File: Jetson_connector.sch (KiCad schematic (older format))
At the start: 24 parts, among them IC2 AT24MAC402-MAHM-T, IC6 SN74AVC1T45DCKT, J2 QTH-060-01-L-D-A, U2 SN74AVC2T45DCUR

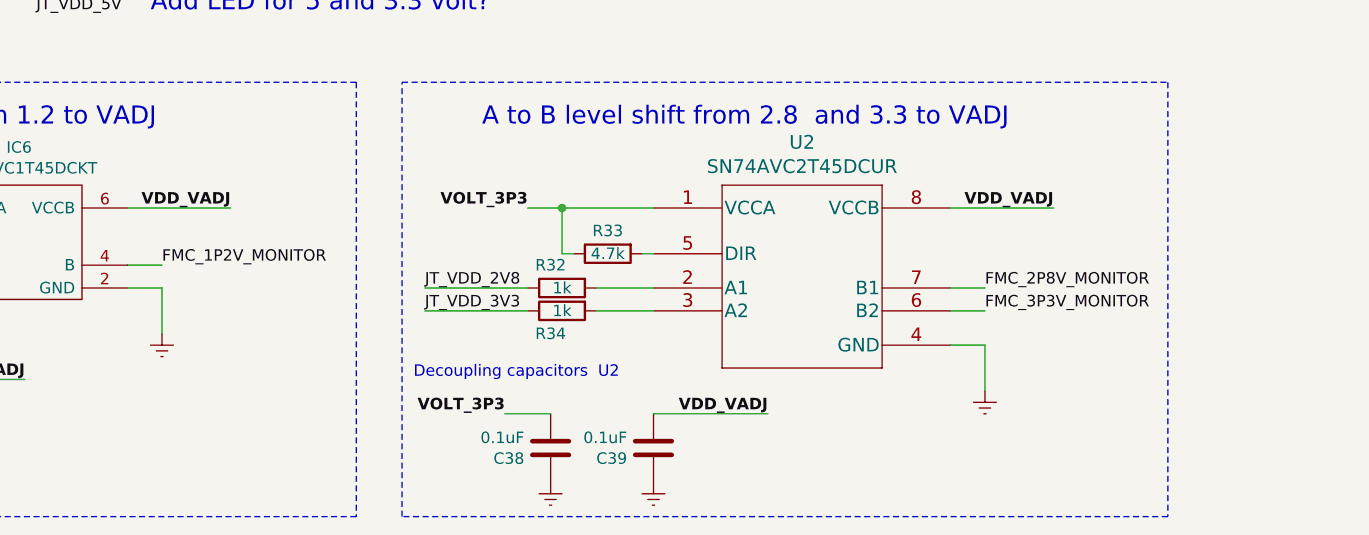
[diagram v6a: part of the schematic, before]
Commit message: Added dummy nets to FMC connector
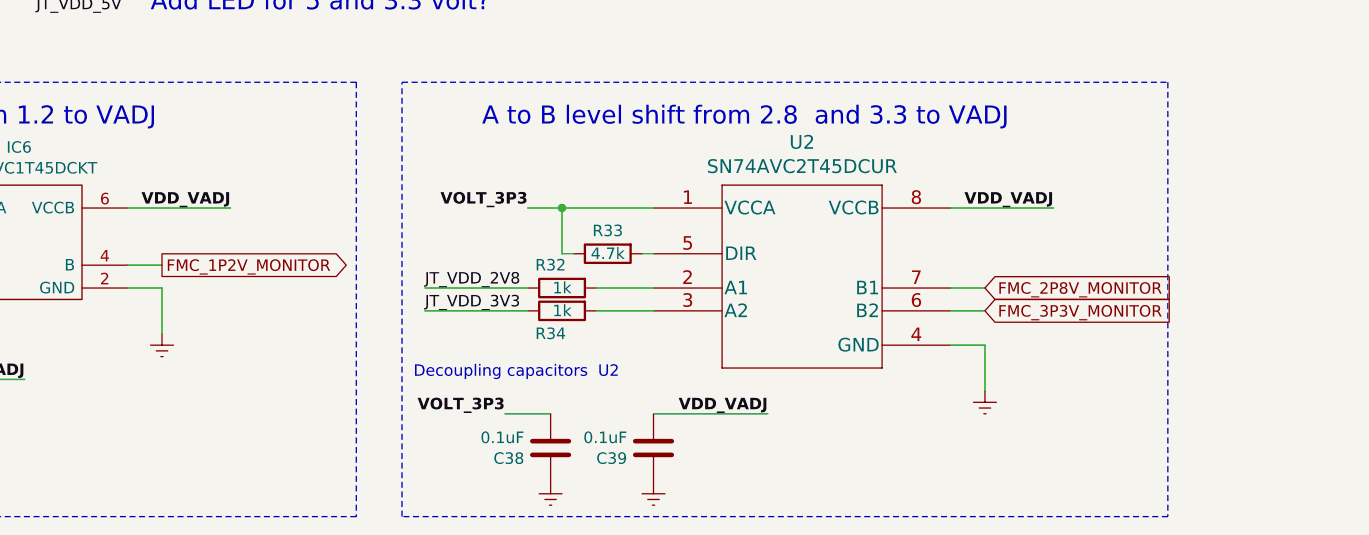
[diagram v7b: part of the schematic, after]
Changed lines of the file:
@@
 Text GLabel 1250 8900 2    50   Output ~ 0
 JT_VDD_1V8
-Text Label 2800 9950 0    50   ~ 0
-FMC_1P2V_MONITOR
 Wire Notes Line
 	600  9150 3650 9150
@@
 Wire Wire Line
 	6250 10050 6400 10050
-Text Label 6400 10050 0    50   ~ 0
-FMC_2P8V_MONITOR
 Wire Notes Line
 	3850 9150 7200 9150
@@
 Wire Wire Line
 	3950 10050 4400 10050
-Text Label 6400 10150 0    50   ~ 0
-FMC_3P3V_MONITOR
 Wire Wire Line
 	6250 10150 6400 10150
@@
 Text Notes 2750 8850 0    79   ~ 0
 Add LED for 5 and 3.3 volt?
+Text GLabel 6400 10050 2    50   Input ~ 0
+FMC_2P8V_MONITOR
+Text GLabel 6400 10150 2    50   Input ~ 0
+FMC_3P3V_MONITOR
+Text GLabel 2800 9950 2    50   Output ~ 0
+FMC_1P2V_MONITOR
 $EndSCHEMATC
